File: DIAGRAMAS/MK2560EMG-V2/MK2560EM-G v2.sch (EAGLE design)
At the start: 76 parts, among them U1 X-MOTOR, U2 Y-MOTOR, U3 Z-MOTOR

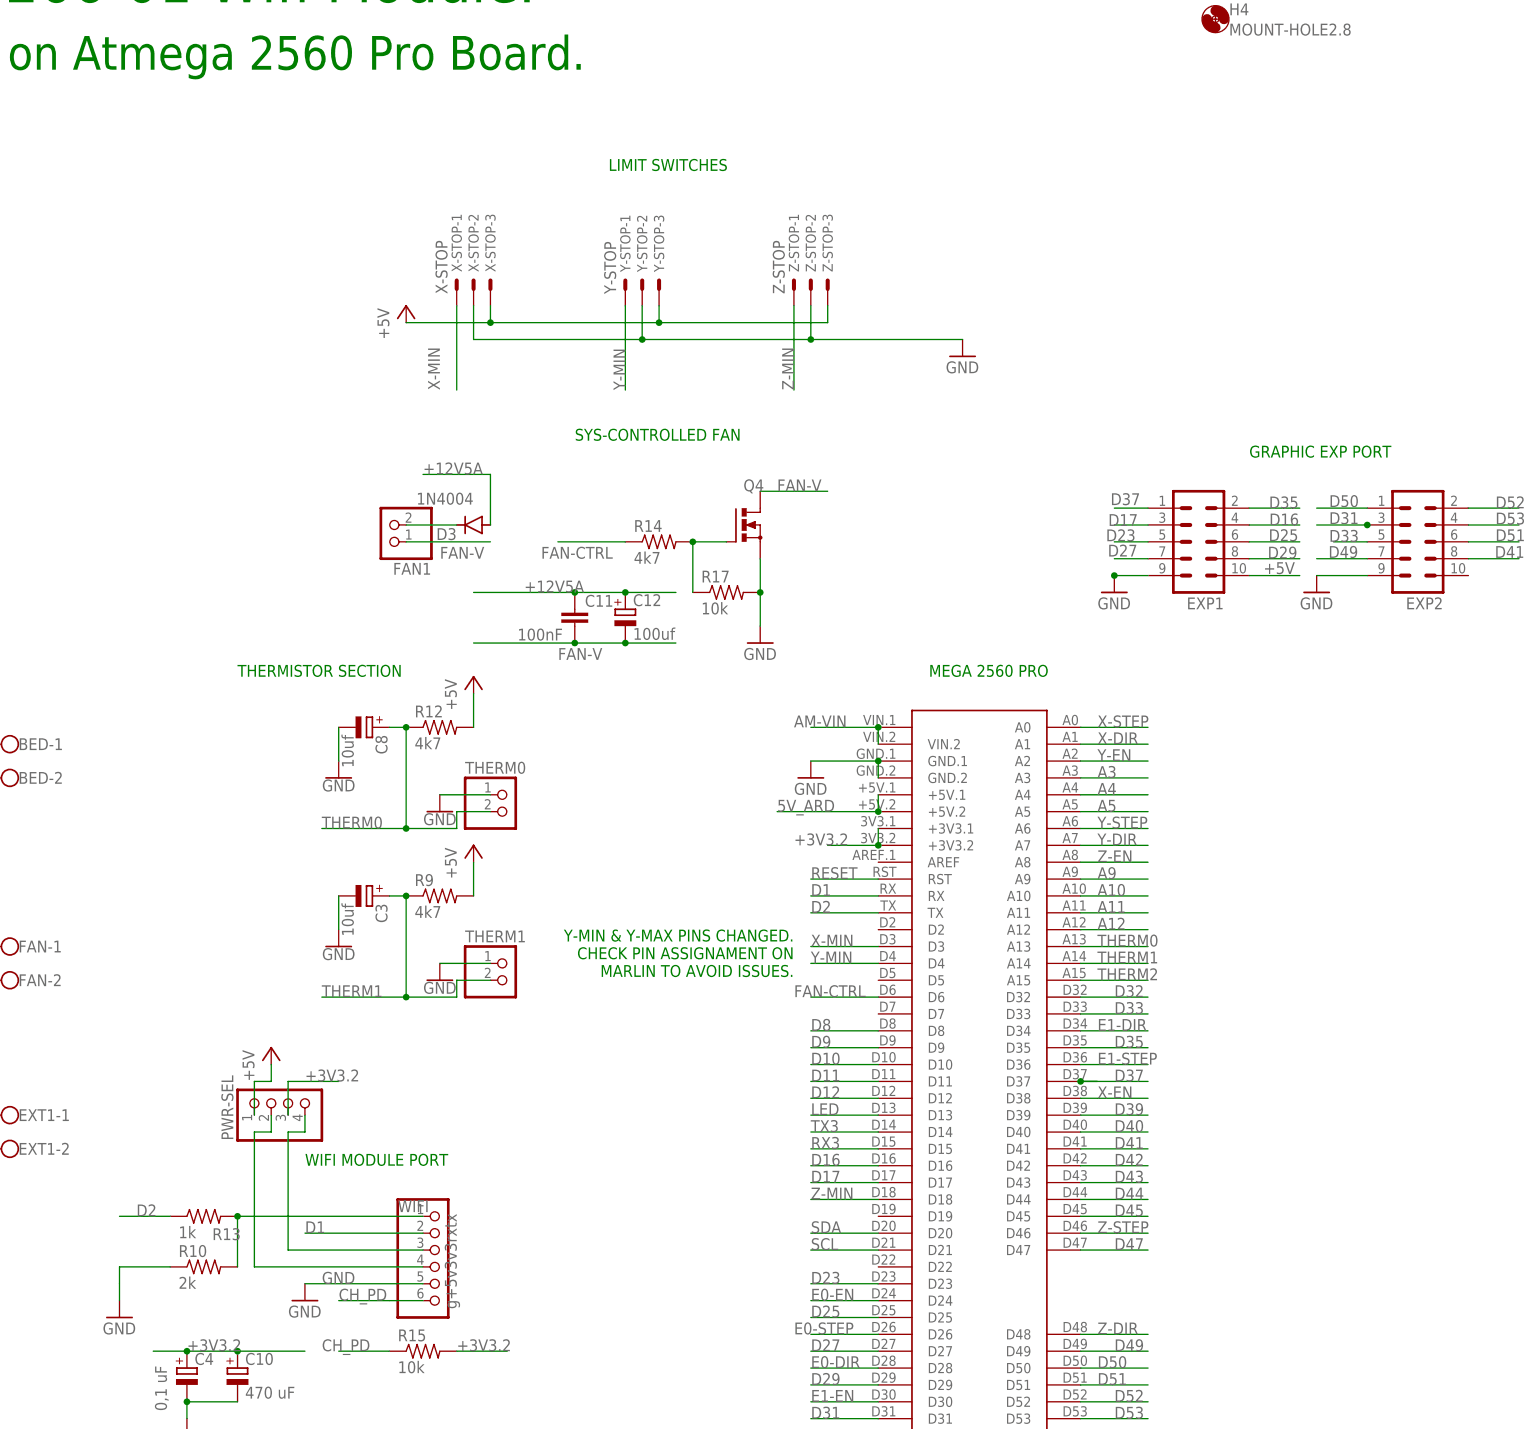
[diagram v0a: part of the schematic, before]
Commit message: pcb minor fix
- optimization and minor pcb fix for better design and perfomance.
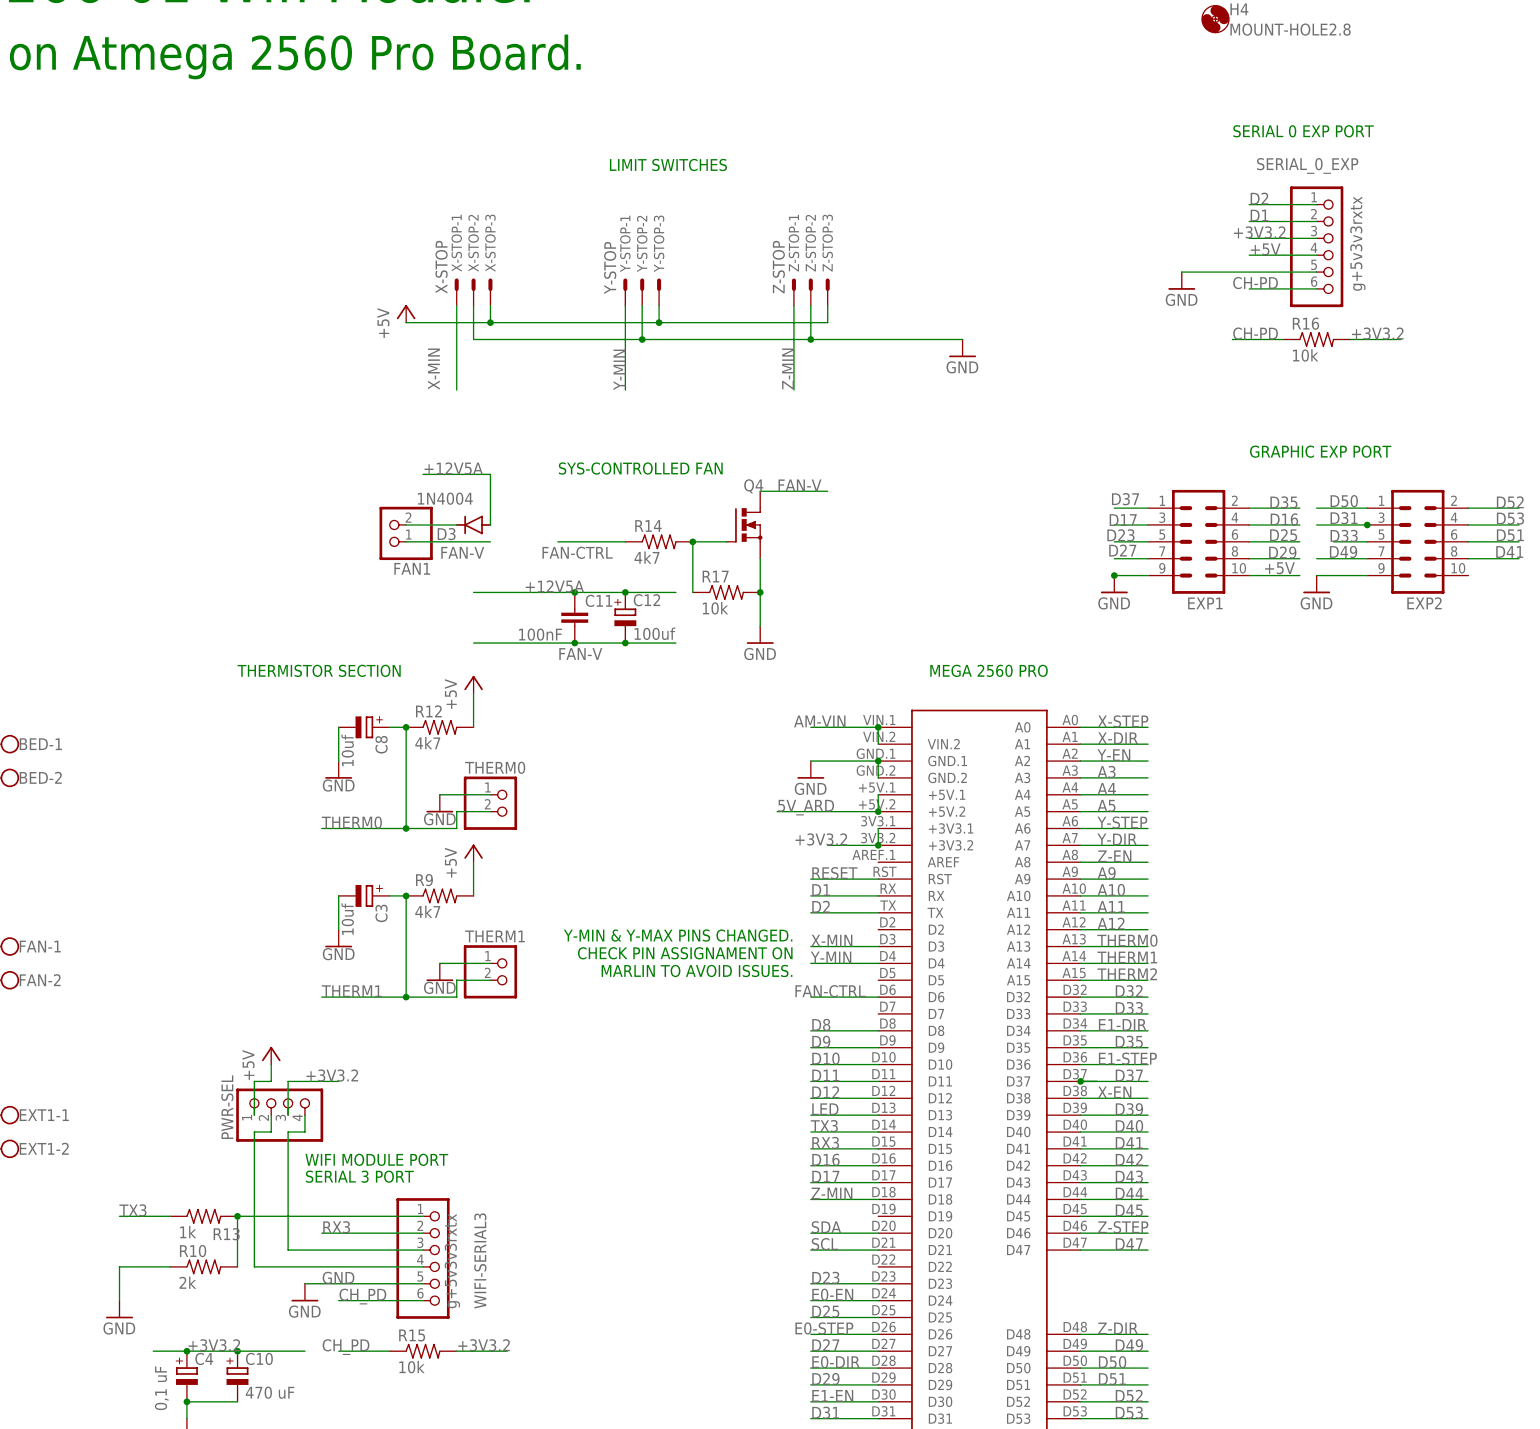
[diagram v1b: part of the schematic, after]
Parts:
- added R16: 10k, resistor:R-US_0204/7
- added SERIAL_0_EXP: g+5v3v3rxtx, pinhead:PINHD-1X6
- renumbered WIFI to WIFI-SERIAL3
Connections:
- new net CH-PD: R16.1, SERIAL_0_EXP.6
- net +3V3.2: now also R16.2, SERIAL_0_EXP.3
- net +5V: now also SERIAL_0_EXP.4
- net D1: now also SERIAL_0_EXP.2; no longer WIFI-SERIAL3.2
- net D2: now also SERIAL_0_EXP.1; no longer R13.1
- net GND: now also SERIAL_0_EXP.5
- net RX3: now also WIFI-SERIAL3.2
- net TX3: now also R13.1
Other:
- note added: "SERIAL 0 EXP PORT"
- note added: "SERIAL 3 PORT"
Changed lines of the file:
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@@
 <part name="12V-IN" library="con-wago-500" library_urn="urn:adsk.eagle:library:195" deviceset="W237-102" device="" package3d_urn="urn:adsk.eagle:package:10688/1"/>
 <part name="PWR-B" library="con-wago-500" library_urn="urn:adsk.eagle:library:195" deviceset="W237-102" device="" package3d_urn="urn:adsk.eagle:package:10688/1"/>
-<part name="WIFI" library="pinhead" library_urn="urn:adsk.eagle:library:325" deviceset="PINHD-1X6" device="" package3d_urn="urn:adsk.eagle:package:22472/2" value="g+5v3v3rxtx"/>
+<part name="WIFI-SERIAL3" library="pinhead" library_urn="urn:adsk.eagle:library:325" deviceset="PINHD-1X6" device="" package3d_urn="urn:adsk.eagle:package:22472/2" value="g+5v3v3rxtx"/>
 <part name="GND24" library="supply1" library_urn="urn:adsk.eagle:library:371" deviceset="GND" device=""/>
 <part name="H1" library="holes" library_urn="urn:adsk.eagle:library:237" deviceset="MOUNT-HOLE" device="2.8" package3d_urn="urn:adsk.eagle:package:14271/1"/>
@@
 <part name="P+4" library="supply1" library_urn="urn:adsk.eagle:library:371" deviceset="+5V" device=""/>
 <part name="PWR-SEL" library="-redpic-connector" deviceset="PINHD-1X4" device=""/>
+<part name="SERIAL_0_EXP" library="pinhead" library_urn="urn:adsk.eagle:library:325" deviceset="PINHD-1X6" device="" package3d_urn="urn:adsk.eagle:package:22472/2" value="g+5v3v3rxtx"/>
+<part name="GND26" library="supply1" library_urn="urn:adsk.eagle:library:371" deviceset="GND" device=""/>
+<part name="R16" library="resistor" deviceset="R-US_" device="0204/7" value="10k"/>
 </parts>
 <sheets>
@@
 <text x="-264.16" y="144.78" size="1.778" layer="91">EXTRUDER MOTOR</text>
 <text x="-55.88" y="251.46" size="1.778" layer="91">LIMIT SWITCHES</text>
-<text x="-60.96" y="210.82" size="1.778" layer="91">SYS-CONTROLLED FAN</text>
+<text x="-63.5" y="205.74" size="1.778" layer="91">SYS-CONTROLLED FAN</text>
 <text x="-241.3" y="254" size="1.778" layer="91">POWER IN</text>
 <text x="-27.94" y="137.16" size="1.778" layer="91" rot="R180">Y-MIN &amp; Y-MAX PINS CHANGED.
@@
 MARLIN TO AVOID ISSUES.</text>
 <text x="-200.66" y="238.76" size="2.54" layer="91">5V-SELECT</text>
+<text x="-101.6" y="99.06" size="1.778" layer="91">SERIAL 3 PORT</text>
+<text x="38.1" y="256.54" size="1.778" layer="91">SERIAL 0 EXP PORT</text>
 </plain>
 <instances>
@@
 <attribute name="NAME" x="-246.38" y="235.331" size="1.778" layer="95"/>
 </instance>
-<instance part="WIFI" gate="A" x="-81.28" y="86.36" smashed="yes">
-<attribute name="NAME" x="-87.63" y="94.615" size="1.778" layer="95"/>
+<instance part="WIFI-SERIAL3" gate="A" x="-81.28" y="86.36" smashed="yes">
+<attribute name="NAME" x="-74.295" y="80.01" size="1.778" layer="95" rot="R90"/>
 <attribute name="VALUE" x="-78.74" y="80.01" size="1.778" layer="96" rot="R90"/>
 </instance>
@@
 <attribute name="NAME" x="-112.395" y="105.41" size="1.778" layer="95" rot="R90"/>
 <attribute name="VALUE" x="-96.52" y="105.41" size="1.778" layer="96" rot="R90"/>
+</instance>
+<instance part="SERIAL_0_EXP" gate="A" x="53.34" y="238.76" smashed="yes">
+<attribute name="NAME" x="57.15" y="253.365" size="1.778" layer="95" rot="R180"/>
+<attribute name="VALUE" x="55.88" y="247.65" size="1.778" layer="96" rot="R270"/>
+</instance>
+<instance part="GND26" gate="1" x="30.48" y="233.68" smashed="yes">
+<attribute name="VALUE" x="27.94" y="231.14" size="1.778" layer="96"/>
+</instance>
+<instance part="R16" gate="G$1" x="50.8" y="226.06" smashed="yes">
+<attribute name="NAME" x="46.99" y="227.5586" size="1.778" layer="95"/>
+<attribute name="VALUE" x="46.99" y="222.758" size="1.778" layer="96"/>
 </instance>
 </instances>
@@
 <label x="-99.06" y="83.82" size="1.778" layer="95"/>
 <pinref part="GND24" gate="1" pin="GND"/>
-<pinref part="WIFI" gate="A" pin="5"/>
+<pinref part="WIFI-SERIAL3" gate="A" pin="5"/>
 <wire x1="-83.82" y1="83.82" x2="-101.6" y2="83.82" width="0.1524" layer="91"/>
 </segment>
@@
 <junction x="-165.1" y="218.44"/>
 </segment>
+<segment>
+<pinref part="SERIAL_0_EXP" gate="A" pin="5"/>
+<pinref part="GND26" gate="1" pin="GND"/>
+<wire x1="50.8" y1="236.22" x2="30.48" y2="236.22" width="0.1524" layer="91"/>
+</segment>
 </net>
 <net name="D1" class="0">
@@
 </segment>
 <segment>
-<pinref part="WIFI" gate="A" pin="2"/>
-<wire x1="-83.82" y1="91.44" x2="-101.6" y2="91.44" width="0.1524" layer="91"/>
-<label x="-101.6" y="91.44" size="1.778" layer="95"/>
+<pinref part="SERIAL_0_EXP" gate="A" pin="2"/>
+<wire x1="50.8" y1="243.84" x2="40.64" y2="243.84" width="0.1524" layer="91"/>
+<label x="40.64" y="243.84" size="1.778" layer="95"/>
 </segment>
 </net>
@@
 </segment>
 <segment>
-<pinref part="R13" gate="G$1" pin="1"/>
-<wire x1="-121.92" y1="93.98" x2="-129.54" y2="93.98" width="0.1524" layer="91"/>
-<label x="-127" y="93.98" size="1.778" layer="95"/>
+<pinref part="SERIAL_0_EXP" gate="A" pin="1"/>
+<wire x1="50.8" y1="246.38" x2="40.64" y2="246.38" width="0.1524" layer="91"/>
+<label x="40.64" y="246.38" size="1.778" layer="95"/>
 </segment>
 </net>
@@
 <pinref part="PWR-SEL" gate="A" pin="1"/>
 <wire x1="-109.22" y1="114.3" x2="-109.22" y2="109.22" width="0.1524" layer="91"/>
+</segment>
+<segment>
+<pinref part="SERIAL_0_EXP" gate="A" pin="4"/>
+<wire x1="50.8" y1="238.76" x2="40.64" y2="238.76" width="0.1524" layer="91"/>
+<label x="40.64" y="238.76" size="1.778" layer="95"/>
 </segment>
 </net>
@@
 <label x="-101.6" y="114.3" size="1.778" layer="95"/>
 </segment>
+<segment>
+<pinref part="SERIAL_0_EXP" gate="A" pin="3"/>
+<wire x1="50.8" y1="241.3" x2="40.64" y2="241.3" width="0.1524" layer="91"/>
+<label x="38.1" y="241.3" size="1.778" layer="95"/>
+</segment>
+<segment>
+<wire x1="55.88" y1="226.06" x2="63.5" y2="226.06" width="0.1524" layer="91"/>
+<pinref part="R16" gate="G$1" pin="2"/>
+<label x="55.88" y="226.06" size="1.778" layer="95"/>
+</segment>
 </net>
 <net name="N$29" class="0">
@@
 <label x="-25.4" y="106.68" size="1.778" layer="95"/>
 </segment>
+<segment>
+<pinref part="R13" gate="G$1" pin="1"/>
+<wire x1="-121.92" y1="93.98" x2="-129.54" y2="93.98" width="0.1524" layer="91"/>
+<label x="-129.54" y="93.98" size="1.778" layer="95"/>
+</segment>
 </net>
 <net name="RX3" class="0">
@@
 <label x="-25.4" y="104.14" size="1.778" layer="95"/>
 </segment>
+<segment>
+<pinref part="WIFI-SERIAL3" gate="A" pin="2"/>
+<wire x1="-83.82" y1="91.44" x2="-99.06" y2="91.44" width="0.1524" layer="91"/>
+<label x="-99.06" y="91.44" size="1.778" layer="95"/>
+</segment>
 </net>
 <net name="CH_PD" class="0">
 <segment>
-<pinref part="WIFI" gate="A" pin="6"/>
+<pinref part="WIFI-SERIAL3" gate="A" pin="6"/>
 <wire x1="-83.82" y1="81.28" x2="-88.9" y2="81.28" width="0.1524" layer="91"/>
 <wire x1="-96.52" y1="81.28" x2="-88.9" y2="81.28" width="0.1524" layer="91"/>
@@
 <net name="N$18" class="0">
 <segment>
-<pinref part="WIFI" gate="A" pin="1"/>
+<pinref part="WIFI-SERIAL3" gate="A" pin="1"/>
 <pinref part="R13" gate="G$1" pin="2"/>
 <wire x1="-83.82" y1="93.98" x2="-111.76" y2="93.98" width="0.1524" layer="91"/>
@@
 <net name="N$31" class="0">
 <segment>
-<pinref part="WIFI" gate="A" pin="4"/>
+<pinref part="WIFI-SERIAL3" gate="A" pin="4"/>
 <wire x1="-83.82" y1="86.36" x2="-109.22" y2="86.36" width="0.1524" layer="91"/>
 <wire x1="-109.22" y1="106.68" x2="-109.22" y2="86.36" width="0.1524" layer="91"/>
@@
 <net name="N$32" class="0">
 <segment>
-<pinref part="WIFI" gate="A" pin="3"/>
+<pinref part="WIFI-SERIAL3" gate="A" pin="3"/>
 <wire x1="-83.82" y1="88.9" x2="-104.14" y2="88.9" width="0.1524" layer="91"/>
 <wire x1="-104.14" y1="106.68" x2="-104.14" y2="88.9" width="0.1524" layer="91"/>
@@
 </segment>
 </net>
+<net name="CH-PD" class="0">
+<segment>
+<pinref part="SERIAL_0_EXP" gate="A" pin="6"/>
+<wire x1="50.8" y1="233.68" x2="40.64" y2="233.68" width="0.1524" layer="91"/>
+<label x="38.1" y="233.68" size="1.778" layer="95"/>
+</segment>
+<segment>
+<wire x1="38.1" y1="226.06" x2="45.72" y2="226.06" width="0.1524" layer="91"/>
+<pinref part="R16" gate="G$1" pin="1"/>
+<label x="38.1" y="226.06" size="1.778" layer="95"/>
+</segment>
+</net>

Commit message: new pcb files
- updated pcb and sch files!
- new improvements and funcionality of the controller board.
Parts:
- added C15, C16, C17: (no value), capacitor-wima:C2.5/2
- added C19, C20, C21: 470uf, rcl:CPOL-EUE2,5-6E
- added FIL-SENS: (no value), -redpic-connector:PINHD-1X3
- added Q5, Q6, Q7: 5.8A/30V/35mΩ, SparkFun-DiscreteSemi:MOSFET-NCH-AO3404A
- added R18, R19, R20, R21, R22, R23: 10k, resistor:R-US_0204/7
- added RGB-LANES: (no value), -redpic-connector:PINHD-1X4
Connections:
- new net B-LED: Q7.G, R20.2
- new net FILM-SENS: ARD-MEGA.D5, FIL-SENS.1
- new net G-LED: Q6.G, R19.2
- new net L-B: C17.1, C21.+, Q7.D, RGB-LANES.3
- new net L-G: C16.1, C19.+, Q6.D, RGB-LANES.2
- new net L-R: C15.1, C20.+, Q5.D, RGB-LANES.1
- new net R-LED: Q5.G, R18.2
- net +5V: now also FIL-SENS.3
- net D43: now also R18.1, R21.1
- net D44: now also R19.1, R22.1
- net D45: now also R20.1, R23.1
- net GND: now also C15.2, C16.2, C17.2, C19.-, C20.-, C21.-, FIL-SENS.2, Q5.S, Q6.S, Q7.S, R21.2, R22.2, R23.2, RGB-LANES.4
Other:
- note added: "Extra Features on Board."
- note added: "FILAMENT SENSOR"
- note added: "FILTERING RGB SIGNAL LINES"
- note added: "RGB LED CONTROL"
- moved on the sheet: 12V-IN-1, 5V_SOURCE, BED-1, BED-2, C1, C10, C11, C12, C13, C14, C2, C3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

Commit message: important pcb update
- added XT60 connectors for bed connection.
- optimization of some pcb tracks, added support for ext reset button.
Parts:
- removed BED, PWR-B: (no value), con-wago-500:W237-102
- added BL-TOUCH, JP1: (no value), -redpic-connector:PINHD-1X2
- added C18: 100nF, capacitor-wima:C2.5/2
- added R24: 10k, resistor:R-US_0204/7
- added U$1, U$2: XT60, XT60:XT60
- C15, C16, C17: value (none) -> 100nF
- PWR-SEL: device -redpic-connector:PINHD-1X4 -> -redpic-connector:PINHD-1X3
- R18, R19, R20: value 10k -> 4k7
- WIFI-SERIAL3: device pinhead:PINHD-1X6 -> pinhead:PINHD-1X5
- renumbered RGB-LANES to RGB-B-G-R
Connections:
- removed net D42: ARD-MEGA.D42
- removed net N$31: PWR-SEL.2, WIFI-SERIAL3.4
- new net D46: ARD-MEGA.D46, R20.1, R23.1
- new net D7: ARD-MEGA.D7, BL-TOUCH.1
- new net N$33: C18.1, JP1.2
- net +12V: now also U$2.VCC; no longer BED-2.KL
- net +5V: now also R24.2
- net CH_PD: now also WIFI-SERIAL3.5; no longer WIFI-SERIAL3.6
- net D43: no longer R18.1, R21.1
- net D44: now also R18.1, R21.1; no longer R19.1, R22.1
- net D45: now also R19.1, R22.1; no longer R20.1, R23.1
- net GND: now also BL-TOUCH.2, C18.2, U$1.GND, WIFI-SERIAL3.4; no longer PWR-B-2.KL, WIFI-SERIAL3.5
- net N$29: now also U$1.VCC; no longer PWR-B-1.KL
- net N$32: now also PWR-SEL.2; no longer PWR-SEL.4
- net N$7: now also U$2.GND; no longer BED-1.KL
- net RESET: now also JP1.1, R24.1
- net Z-STEP: now also ARD-MEGA.D42; no longer ARD-MEGA.D46
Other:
- note added: "BL TOUCH EXTRA PINS"
- note added: "MCU DIODE PROTECTION"
- note added: "MikroPrintr MK2560EM-G Rev. 2 Support for RepRap Smart Controller and ESP-8266-01s Wifi Module."
- note added: "RESET EXT HEADER"
- note removed: "DIODE PROTECTION"
- note removed: "MikroPrintr MK2560EM-G Rev. 1G.1 Support for RepRap Smart Controller and ESP-8266-01 Wifi Module."
- moved on the sheet: C11, C12, C15, C16, C17, C19, C20, C21
